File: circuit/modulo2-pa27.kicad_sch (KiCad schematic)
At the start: 48 parts, among them J1 CONN_01X02, J3 CONN_01X04, J4 JACK_MONO, J5 HOLE, J7 HOLE, SW1 bright, U1 OPA2134, U2 OPA2134, U3 TLE2426, U4 PWR_CONN

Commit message: almost there...
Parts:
- C3, C8: footprint myAmp:C_FILM_L7.2mm_W5.5mm_P5.00mm -> myAmp:C_FILM_L7.2mm_W5.0mm_P5.00mm
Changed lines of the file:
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@@
     (property "Reference" "C8" (id 0) (at 156.21 67.31 0))
     (property "Value" "1µF" (id 1) (at 156.21 69.85 0))
-    (property "Footprint" "myAmp:C_FILM_L7.2mm_W5.5mm_P5.00mm" (id 2) (at 151.4348 64.77 0)
+    (property "Footprint" "myAmp:C_FILM_L7.2mm_W5.0mm_P5.00mm" (id 2) (at 151.4348 64.77 0)
       (effects (font (size 1.27 1.27)) hide)
     )
@@
     (property "Reference" "C3" (id 0) (at 86.36 66.04 0))
     (property "Value" "1µF" (id 1) (at 86.36 68.58 0))
-    (property "Footprint" "myAmp:C_FILM_L7.2mm_W5.5mm_P5.00mm" (id 2) (at 81.5848 63.5 0)
+    (property "Footprint" "myAmp:C_FILM_L7.2mm_W5.0mm_P5.00mm" (id 2) (at 81.5848 63.5 0)
       (effects (font (size 1.27 1.27)) hide)
     )
@@
     )
     (path "/66f613c0-61ed-40a1-a380-fef466742922"
-      (reference "C3") (unit 1) (value "1µF") (footprint "myAmp:C_FILM_L7.2mm_W5.5mm_P5.00mm")
+      (reference "C3") (unit 1) (value "1µF") (footprint "myAmp:C_FILM_L7.2mm_W5.0mm_P5.00mm")
     )
     (path "/48142eaa-7210-4390-91e8-e59685a2b4d4"
@@
     )
     (path "/11af6226-d94c-469b-95d8-d952d2567f76"
-      (reference "C8") (unit 1) (value "1µF") (footprint "myAmp:C_FILM_L7.2mm_W5.5mm_P5.00mm")
+      (reference "C8") (unit 1) (value "1µF") (footprint "myAmp:C_FILM_L7.2mm_W5.0mm_P5.00mm")
     )
     (path "/5b89da72-879f-440b-96c6-c1f1e0879801"

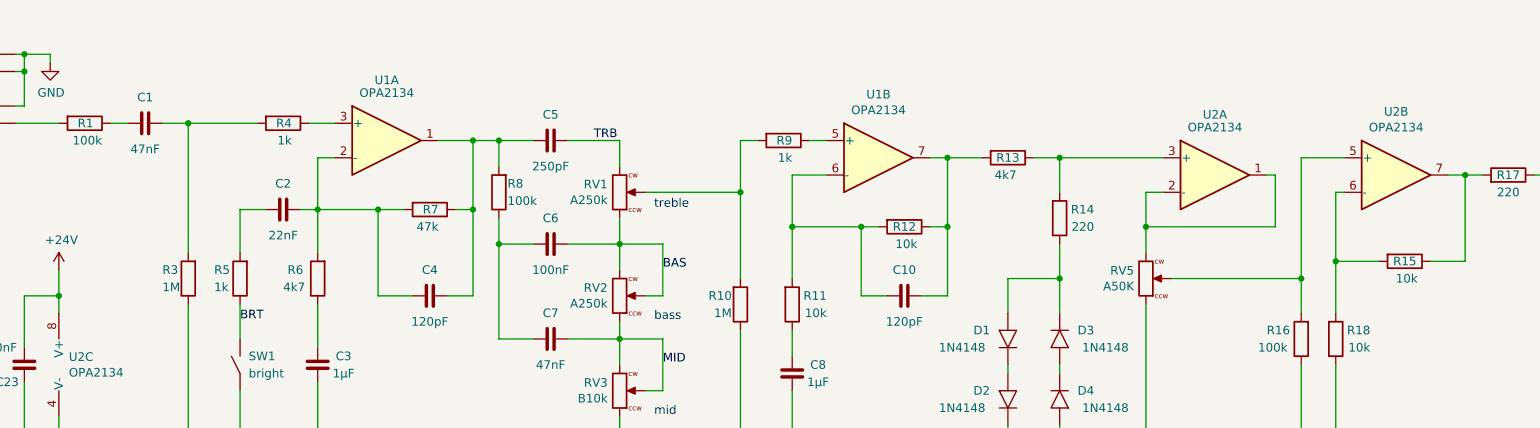
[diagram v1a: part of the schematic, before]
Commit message: fixed mistakes from assembly; added bootloader; firmware changed for PCB
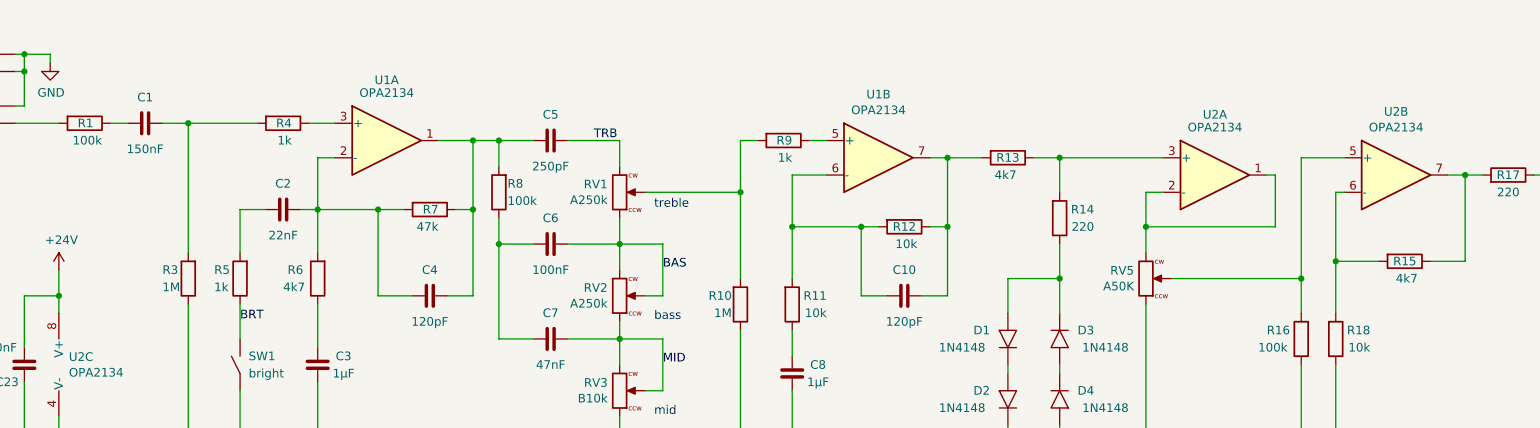
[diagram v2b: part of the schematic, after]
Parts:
- C1: value 47nF -> 150nF
- C5: footprint myAmp:C_FILM_L7.2mm_W3.5mm_P5.00mm -> myAmp:C_2.5MM
- R15: value 10k -> 4k7
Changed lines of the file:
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@@
     (in_bom yes) (on_board yes)
     (property "Reference" "C1" (id 0) (at 57.15 27.94 90))
-    (property "Value" "47nF" (id 1) (at 57.15 35.56 90))
+    (property "Value" "150nF" (id 1) (at 57.15 35.56 90))
     (property "Footprint" "myAmp:C_FILM_L7.2mm_W3.5mm_P5.00mm" (id 2) (at 60.96 30.7848 0)
       (effects (font (size 1.27 1.27)) hide)
@@
     (property "Reference" "C5" (id 0) (at 116.84 30.48 90))
     (property "Value" "250pF" (id 1) (at 116.84 38.1 90))
-    (property "Footprint" "myAmp:C_FILM_L7.2mm_W3.5mm_P5.00mm" (id 2) (at 120.65 33.3248 0)
+    (property "Footprint" "myAmp:C_2.5MM" (id 2) (at 120.65 33.3248 0)
       (effects (font (size 1.27 1.27)) hide)
     )
@@
     (in_bom yes) (on_board yes)
     (property "Reference" "R15" (id 0) (at 242.57 52.07 90))
-    (property "Value" "10k" (id 1) (at 244.475 54.61 90)
+    (property "Value" "4k7" (id 1) (at 244.475 54.61 90)
       (effects (font (size 1.27 1.27)) (justify right))
     )
@@
     )
     (path "/00000000-0000-0000-0000-000061baa65d"
-      (reference "C1") (unit 1) (value "47nF") (footprint "myAmp:C_FILM_L7.2mm_W3.5mm_P5.00mm")
+      (reference "C1") (unit 1) (value "150nF") (footprint "myAmp:C_FILM_L7.2mm_W3.5mm_P5.00mm")
     )
     (path "/ae2e9d4a-7d99-4f91-b532-5d8ec352d108"
@@
     )
     (path "/00000000-0000-0000-0000-000061c307c0"
-      (reference "C5") (unit 1) (value "250pF") (footprint "myAmp:C_FILM_L7.2mm_W3.5mm_P5.00mm")
+      (reference "C5") (unit 1) (value "250pF") (footprint "myAmp:C_2.5MM")
     )
     (path "/00000000-0000-0000-0000-000061c52359"
@@
     )
     (path "/528c4caa-abd9-4c76-a2f9-5cc7d77f317f"
-      (reference "R15") (unit 1) (value "10k") (footprint "myAmp:R_10MM")
+      (reference "R15") (unit 1) (value "4k7") (footprint "myAmp:R_10MM")
     )
     (path "/8b87a0e2-0d4e-4917-8cb8-8611032f3b61"

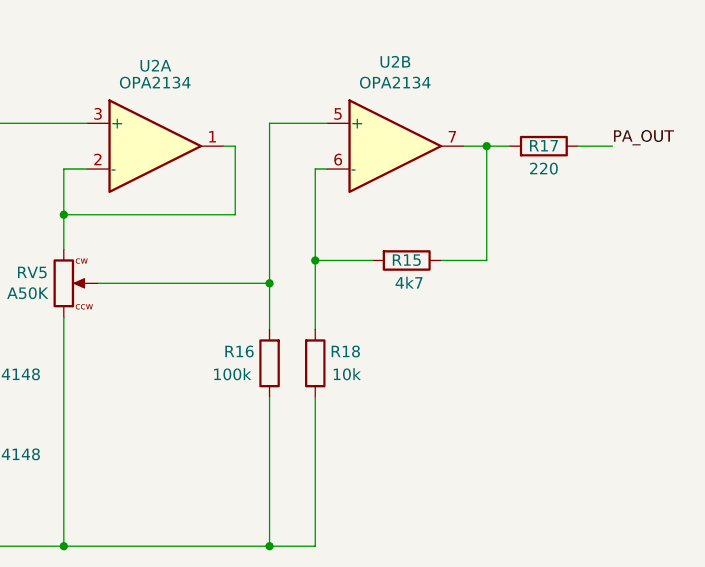
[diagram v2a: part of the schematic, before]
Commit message: reduced preamp gain to not clip the FV-1; timer_ticks_high();
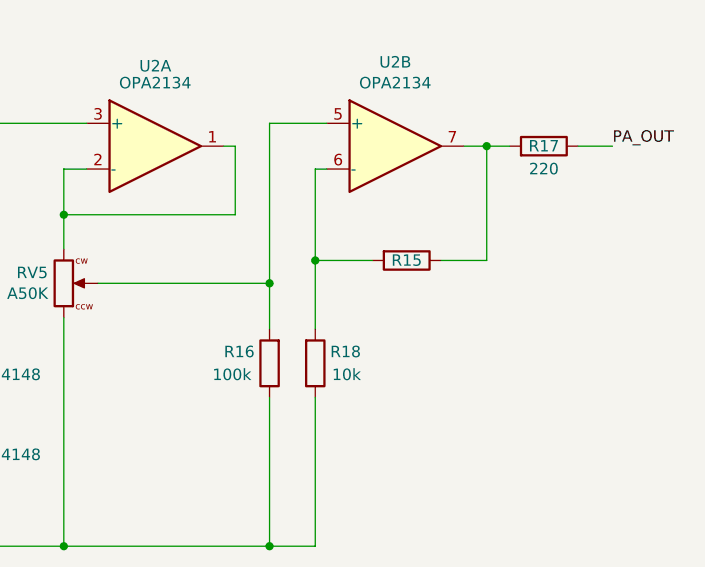
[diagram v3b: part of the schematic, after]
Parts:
- R15: value 4k7 -> (none)
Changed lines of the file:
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@@
       (effects (font (size 1.27 1.27)) hide)
     )
+    (pin "1")
+    (pin "2")
+    (pin "3")
+    (pin "5")
+    (pin "6")
+    (pin "7")
     (pin "4")
     (pin "8")
@@
     (pin "2")
     (pin "3")
+    (pin "5")
+    (pin "6")
+    (pin "7")
+    (pin "4")
+    (pin "8")
   )
   (symbol (lib_id "power:+24V") (at 24.13 53.34 0) (unit 1)
@@
       (effects (font (size 1.27 1.27)) hide)
     )
+    (pin "1")
+    (pin "2")
+    (pin "3")
     (pin "5")
     (pin "6")
     (pin "7")
+    (pin "4")
+    (pin "8")
   )
   (symbol (lib_id "myAmp:1N4148") (at 191.77 72.39 270) (unit 1)
@@
     (pin "2")
     (pin "3")
+    (pin "5")
+    (pin "6")
+    (pin "7")
+    (pin "4")
+    (pin "8")
   )
   (symbol (lib_id "power:GND") (at 92.71 127 270) (mirror x) (unit 1)
@@
     (in_bom yes) (on_board yes)
     (property "Reference" "R15" (id 0) (at 242.57 52.07 90))
-    (property "Value" "4k7" (id 1) (at 244.475 54.61 90)
+    (property "Value" "" (id 1) (at 244.475 54.61 90)
       (effects (font (size 1.27 1.27)) (justify right))
     )
@@
       (effects (font (size 1.27 1.27)) hide)
     )
+    (pin "1")
+    (pin "2")
+    (pin "3")
     (pin "5")
     (pin "6")
     (pin "7")
+    (pin "4")
+    (pin "8")
   )
   (symbol (lib_id "myAmp:R") (at 184.15 36.83 270) (unit 1)
@@
       (effects (font (size 1.27 1.27)) hide)
     )
+    (pin "1")
+    (pin "2")
+    (pin "3")
+    (pin "5")
+    (pin "6")
+    (pin "7")
     (pin "4")
     (pin "8")
@@
     )
     (path "/528c4caa-abd9-4c76-a2f9-5cc7d77f317f"
-      (reference "R15") (unit 1) (value "4k7") (footprint "myAmp:R_10MM")
+      (reference "R15") (unit 1) (value "2k2") (footprint "myAmp:R_10MM")
     )
     (path "/8b87a0e2-0d4e-4917-8cb8-8611032f3b61"
